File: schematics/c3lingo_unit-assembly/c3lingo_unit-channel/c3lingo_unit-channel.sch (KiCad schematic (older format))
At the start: 124 parts, among them J301 Mic X In, J302 Headphone X, J303 PowerSupply, J304 Inputs, J305 Output, J306 PowerSupply, J307 Interconnect, J308 Interconnect, SW301 OnAir_X, SW302 Mute_X, U301 NE5534, U302 LM833N, U303 LM386N-4, U304 LM833N, U305 LM339, U306 LM339, U307 LM339

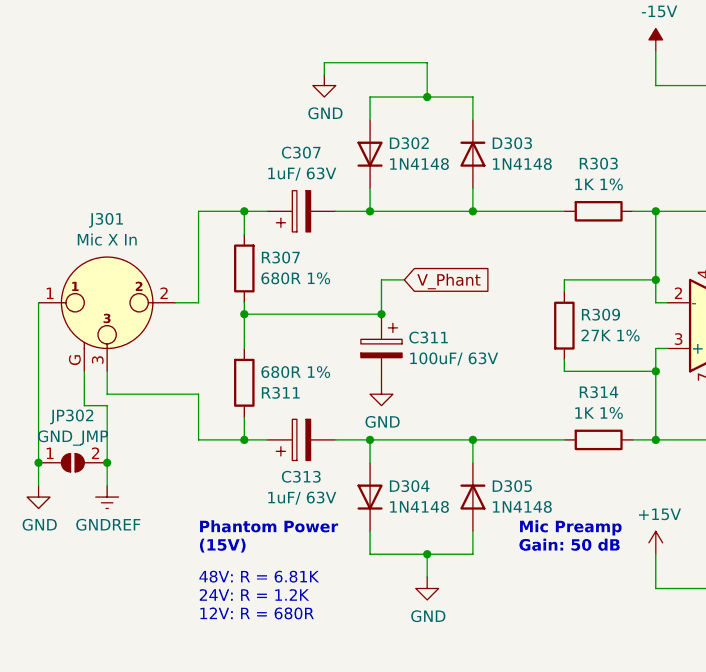
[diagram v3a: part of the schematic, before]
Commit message: PCB: Channel strip design
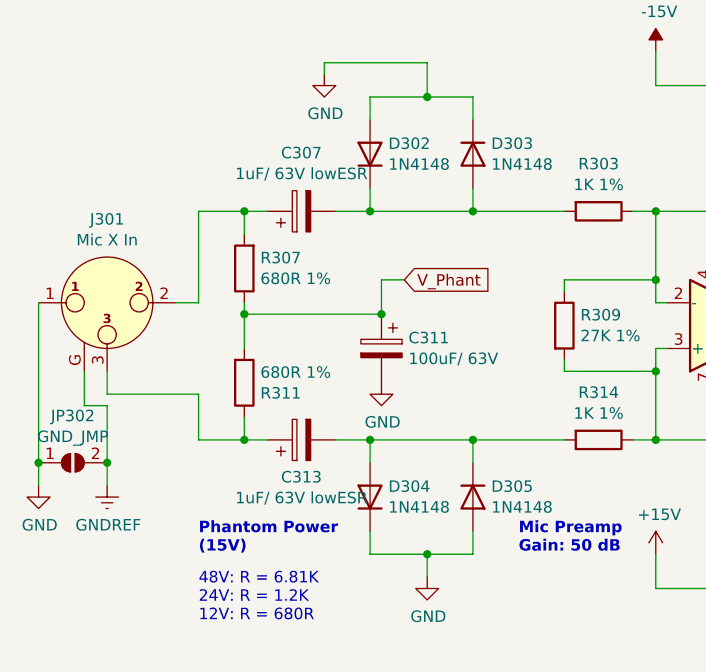
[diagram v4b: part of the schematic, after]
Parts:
- C301, C302, C308, C311, C318: Model 25V -> (none)
- C307, C313: value 1uF/ 63V -> 1uF/ 63V lowESR; Model 16V low ESR electrolytic // plastic film -> low ESR electrolytic // plastic film
- C310: Model 16V low ESR -> (none)
- U301, U302, U303, U304: Model (none) -> +DIP-8 Socket
- U305, U306, U307: Model (none) -> +DIP-14 Socket
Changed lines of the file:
@@
 F 2 "Package_DIP:DIP-14_W7.62mm_Socket_LongPads" H 7050 8500 50  0001 C CNN
 F 3 "https://www.ti.com/lit/ds/symlink/lm339.pdf" H 7150 8600 50  0001 C CNN
+F 4 "+DIP-14 Socket" H 7100 8400 50  0001 C CNN "Model"
 	5    7100 8400
 	0    -1   -1   0
@@
 F 2 "Package_DIP:DIP-14_W7.62mm_Socket_LongPads" H 9650 8500 50  0001 C CNN
 F 3 "https://www.ti.com/lit/ds/symlink/lm339.pdf" H 9750 8600 50  0001 C CNN
+F 4 "+DIP-14 Socket" H 9700 8400 50  0001 C CNN "Model"
 	5    9700 8400
 	0    -1   -1   0
@@
 F 2 "Package_DIP:DIP-14_W7.62mm_Socket_LongPads" H 12250 8500 50  0001 C CNN
 F 3 "https://www.ti.com/lit/ds/symlink/lm339.pdf" H 12350 8600 50  0001 C CNN
+F 4 "+DIP-14 Socket" H 12300 8400 50  0001 C CNN "Model"
 	5    12300 8400
 	0    -1   -1   0
@@
 F 2 "Package_DIP:DIP-8_W7.62mm_Socket_LongPads" H 3050 8600 50  0001 C CNN
 F 3 "https://www.ti.com/lit/ds/symlink/lm833.pdf" H 3050 8600 50  0001 C CNN
+F 4 "+DIP-8 Socket" H 3050 8600 50  0001 C CNN "Model"
 	3    3050 8600
 	0    1    1    0
@@
 F 2 "Package_DIP:DIP-8_W7.62mm_Socket_LongPads" H 3100 7500 50  0001 C CNN
 F 3 "https://www.ti.com/lit/ds/symlink/lm833.pdf" H 3100 7500 50  0001 C CNN
+F 4 "+DIP-8 Socket" H 3100 7500 50  0001 C CNN "Model"
 	2    3100 7500
 	1    0    0    1
@@
 F 2 "Package_DIP:DIP-14_W7.62mm_Socket_LongPads" H 6750 7200 50  0001 C CNN
 F 3 "https://www.ti.com/lit/ds/symlink/lm339.pdf" H 6850 7300 50  0001 C CNN
+F 4 "+DIP-14 Socket" H 6800 7100 50  0001 C CNN "Model"
 	3    6800 7100
 	0    -1   -1   0
@@
 F 2 "Package_DIP:DIP-14_W7.62mm_Socket_LongPads" H 7400 7200 50  0001 C CNN
 F 3 "https://www.ti.com/lit/ds/symlink/lm339.pdf" H 7500 7300 50  0001 C CNN
+F 4 "+DIP-14 Socket" H 7450 7100 50  0001 C CNN "Model"
 	2    7450 7100
 	0    -1   -1   0
@@
 F 2 "Package_DIP:DIP-14_W7.62mm_Socket_LongPads" H 8050 7200 50  0001 C CNN
 F 3 "https://www.ti.com/lit/ds/symlink/lm339.pdf" H 8150 7300 50  0001 C CNN
+F 4 "+DIP-14 Socket" H 8100 7100 50  0001 C CNN "Model"
 	1    8100 7100
 	0    -1   -1   0
@@
 F 2 "Package_DIP:DIP-14_W7.62mm_Socket_LongPads" H 8700 7200 50  0001 C CNN
 F 3 "https://www.ti.com/lit/ds/symlink/lm339.pdf" H 8800 7300 50  0001 C CNN
+F 4 "+DIP-14 Socket" H 8750 7100 50  0001 C CNN "Model"
 	4    8750 7100
 	0    -1   -1   0
@@
 F 2 "Package_DIP:DIP-14_W7.62mm_Socket_LongPads" H 9350 7200 50  0001 C CNN
 F 3 "https://www.ti.com/lit/ds/symlink/lm339.pdf" H 9450 7300 50  0001 C CNN
+F 4 "+DIP-14 Socket" H 9400 7100 50  0001 C CNN "Model"
 	3    9400 7100
 	0    -1   -1   0
@@
 F 2 "Package_DIP:DIP-14_W7.62mm_Socket_LongPads" H 10000 7200 50  0001 C CNN
 F 3 "https://www.ti.com/lit/ds/symlink/lm339.pdf" H 10100 7300 50  0001 C CNN
+F 4 "+DIP-14 Socket" H 10050 7100 50  0001 C CNN "Model"
 	2    10050 7100
 	0    -1   -1   0
@@
 F 2 "Package_DIP:DIP-14_W7.62mm_Socket_LongPads" H 10650 7200 50  0001 C CNN
 F 3 "https://www.ti.com/lit/ds/symlink/lm339.pdf" H 10750 7300 50  0001 C CNN
+F 4 "+DIP-14 Socket" H 10700 7100 50  0001 C CNN "Model"
 	1    10700 7100
 	0    -1   -1   0
@@
 F 2 "Package_DIP:DIP-14_W7.62mm_Socket_LongPads" H 11300 7200 50  0001 C CNN
 F 3 "https://www.ti.com/lit/ds/symlink/lm339.pdf" H 11400 7300 50  0001 C CNN
+F 4 "+DIP-14 Socket" H 11350 7100 50  0001 C CNN "Model"
 	4    11350 7100
 	0    -1   -1   0
@@
 F 2 "Package_DIP:DIP-14_W7.62mm_Socket_LongPads" H 11950 7200 50  0001 C CNN
 F 3 "https://www.ti.com/lit/ds/symlink/lm339.pdf" H 12050 7300 50  0001 C CNN
+F 4 "+DIP-14 Socket" H 12000 7100 50  0001 C CNN "Model"
 	3    12000 7100
 	0    -1   -1   0
@@
 F 2 "Package_DIP:DIP-14_W7.62mm_Socket_LongPads" H 12600 7200 50  0001 C CNN
 F 3 "https://www.ti.com/lit/ds/symlink/lm339.pdf" H 12700 7300 50  0001 C CNN
+F 4 "+DIP-14 Socket" H 12650 7100 50  0001 C CNN "Model"
 	2    12650 7100
 	0    -1   -1   0
@@
 F 2 "Package_DIP:DIP-14_W7.62mm_Socket_LongPads" H 13250 7200 50  0001 C CNN
 F 3 "https://www.ti.com/lit/ds/symlink/lm339.pdf" H 13350 7300 50  0001 C CNN
+F 4 "+DIP-14 Socket" H 13300 7100 50  0001 C CNN "Model"
 	1    13300 7100
 	0    -1   -1   0
@@
 AR Path="/600A9821" Ref="C113"  Part="1"
 F 0 "C313" V 1587 3500 50  0000 C CNN
-F 1 "1uF/ 63V" V 1496 3500 50  0000 C CNN
+F 1 "1uF/ 63V lowESR" V 1496 3500 50  0000 C CNN
 F 2 "Capacitor_THT:CP_Radial_D5.0mm_P2.00mm" H 1788 3350 50  0001 C CNN
 F 3 "~" H 1750 3500 50  0001 C CNN
-F 4 "16V low ESR electrolytic // plastic film" H 1750 3500 50  0001 C CNN "Model"
+F 4 "low ESR electrolytic // plastic film" H 1750 3500 50  0001 C CNN "Model"
 	1    1750 3500
 	0    -1   -1   0
@@
 AR Path="/5FF457A4" Ref="C107"  Part="1"
 F 0 "C307" V 2005 2500 50  0000 C CNN
-F 1 "1uF/ 63V" V 1914 2500 50  0000 C CNN
+F 1 "1uF/ 63V lowESR" V 1914 2500 50  0000 C CNN
 F 2 "Capacitor_THT:CP_Radial_D5.0mm_P2.00mm" H 1788 2350 50  0001 C CNN
 F 3 "~" H 1750 2500 50  0001 C CNN
-F 4 "16V low ESR electrolytic // plastic film" H 1750 2500 50  0001 C CNN "Model"
+F 4 "low ESR electrolytic // plastic film" H 1750 2500 50  0001 C CNN "Model"
 	1    1750 2500
 	0    -1   -1   0
@@
 F 2 "Capacitor_THT:CP_Radial_D10.0mm_P5.00mm" H 2138 2950 50  0001 C CNN
 F 3 "~" H 2100 3100 50  0001 C CNN
-F 4 "25V" H 2100 3100 50  0001 C CNN "Model"
+F 4 "" H 2100 3100 50  0001 C CNN "Model"
 	1    2100 3100
 	-1   0    0    -1
@@
 F 2 "Package_DIP:DIP-8_W7.62mm_Socket_LongPads" H 11750 3000 50  0001 C CNN
 F 3 "https://www.ti.com/lit/ds/symlink/lm833.pdf" H 11750 3000 50  0001 C CNN
+F 4 "+DIP-8 Socket" H 11750 3000 50  0001 C CNN "Model"
 	2    11750 3000
 	1    0    0    1
@@
 F 2 "Package_DIP:DIP-8_W7.62mm_Socket_LongPads" H 14100 3100 50  0001 C CNN
 F 3 "https://www.ti.com/lit/ds/symlink/lm386.pdf" H 14200 3200 50  0001 C CNN
+F 4 "+DIP-8 Socket" H 14000 3000 50  0001 C CNN "Model"
 	1    14000 3000
 	1    0    0    -1
@@
 F 2 "Capacitor_THT:CP_Radial_D6.3mm_P2.50mm" H 14488 1650 50  0001 C CNN
 F 3 "~" H 14450 1800 50  0001 C CNN
-F 4 "25V" H 14450 1800 50  0001 C CNN "Model"
+F 4 "" H 14450 1800 50  0001 C CNN "Model"
 	1    14450 1800
 	0    -1   1    0
@@
 F 2 "Capacitor_THT:CP_Radial_D6.3mm_P2.50mm" H 14188 2400 50  0001 C CNN
 F 3 "~" H 14150 2550 50  0001 C CNN
-F 4 "25V" H 14150 2550 50  0001 C CNN "Model"
+F 4 "" H 14150 2550 50  0001 C CNN "Model"
 	1    14150 2550
 	0    -1   -1   0
@@
 F 2 "Capacitor_THT:CP_Radial_D6.3mm_P2.50mm" H 15088 2850 50  0001 C CNN
 F 3 "~" H 15050 3000 50  0001 C CNN
-F 4 "16V low ESR" H 15050 3000 50  0001 C CNN "Model"
+F 4 "" H 15050 3000 50  0001 C CNN "Model"
 	1    15050 3000
 	0    -1   -1   0
@@
 F 2 "Package_DIP:DIP-8_W7.62mm_Socket_LongPads" H 6800 3250 50  0001 C CNN
 F 3 "https://www.ti.com/lit/ds/symlink/lm833.pdf" H 6800 3250 50  0001 C CNN
+F 4 "+DIP-8 Socket" H 6800 3250 50  0001 C CNN "Model"
 	1    6800 3250
 	1    0    0    1
@@
 F 2 "Package_DIP:DIP-8_W7.62mm_Socket_LongPads" H 8300 4000 50  0001 C CNN
 F 3 "https://www.ti.com/lit/ds/symlink/lm833.pdf" H 8300 4000 50  0001 C CNN
+F 4 "+DIP-8 Socket" H 8300 4000 50  0001 C CNN "Model"
 	3    8300 4000
 	0    1    1    0
@@
 F 2 "Package_DIP:DIP-8_W7.62mm_Socket_LongPads" H 3700 3050 50  0001 C CNN
 F 3 "https://www.ti.com/lit/ds/symlink/ne5534.pdf" H 3700 3150 50  0001 C CNN
+F 4 "+DIP-8 Socket" H 3650 3000 50  0001 C CNN "Model"
 	1    3650 3000
 	1    0    0    1
@@
 F 2 "Capacitor_THT:CP_Radial_D6.3mm_P2.50mm" H 4188 1650 50  0001 C CNN
 F 3 "~" H 4150 1800 50  0001 C CNN
-F 4 "25V" H 4150 1800 50  0001 C CNN "Model"
+F 4 "" H 4150 1800 50  0001 C CNN "Model"
 	1    4150 1800
 	0    1    -1   0
@@
 F 2 "Capacitor_THT:CP_Radial_D6.3mm_P2.50mm" H 4188 4150 50  0001 C CNN
 F 3 "~" H 4150 4300 50  0001 C CNN
-F 4 "25V" H 4150 4300 50  0001 C CNN "Model"
+F 4 "" H 4150 4300 50  0001 C CNN "Model"
 	1    4150 4300
 	0    -1   1    0
@@
 F 2 "Package_DIP:DIP-14_W7.62mm_Socket_LongPads" H 6100 7200 50  0001 C CNN
 F 3 "https://www.ti.com/lit/ds/symlink/lm339.pdf" H 6200 7300 50  0001 C CNN
+F 4 "+DIP-14 Socket" H 6150 7100 50  0001 C CNN "Model"
 	4    6150 7100
 	0    -1   -1   0

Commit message: [FIX] Schematics: Revised values and PCB errata text
* fixed trim pot range at VU meter
* TODOs removed (5V V_LED didn't work out, 10uF at LM386 wasn't better, VU meter filtering not needed)
* phantom power voltage changed and readme chapter added
* hardware errata: gain pot. pins are swapped, ground plane isn't fully connected

Footprints and PCB aren't fixed to keep the schematic compatible with the existing PCBs!
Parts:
- R307, R311: value 680R 1% -> 6.8K 1%
- R320: value 3.9K -> 15K
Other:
- note added: "Bridge V_LED to +15V\n(5V V_LED didn’t work)"
- note added: "Buffer/ Rectifier\nGain: 15\n(3.9 + 12 dB for\ntrim pot. headroom)"
- note added: "DNP R312 and\nreplace C309 with\na jumper!"
- note added: "PCB Errata:\n- R302 (R102 on PCB) has pins 1 and 3 swapped. Connect R305 (R105) directly to the left\n potentiometer pin!\n- The ground plane at the headphone mix potentiometers is not connected to the remaining\n ground plane/ power input. Place a jumper manually!"
- note added: "Phantom Power\n(48V)"
- note added: "Signal Smoothing\n==> DNP (not required)"
- note removed: "Buffer/ Rectifier\nGain: 3.9"
- note removed: "Phantom Power\n(15V)"
- note removed: "Signal Smoothing\nTODO: Remove all together!?"
- note removed: "TODO: Change to 10 uF?"
- note removed: "TODO: Try with V_LED = 5V\nrd: 2.3 V (390R @15V)\ngn: 2.4 V (390R @15V)\nye: 2.6 V (390R @15V)"
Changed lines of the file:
@@
 Sheet 3 5
 Title "c3lingo interpeter unit -- channel strip"
-Date "2021-05-28"
-Rev "v0.2"
+Date "2021-09-02"
+Rev "v0.2.1"
 Comp "Jannik Beyerstedt (jtbx)"
-Comment1 "Prototype 1"
+Comment1 "Prototype 1 (with errata)"
 Comment2 ""
 Comment3 ""
@@
 	0    -1   -1   0
 $EndComp
-Text Notes 1850 7900 0    50   ~ 0
-Buffer/ Rectifier\nGain: 3.9
+Text Notes 1850 8000 0    50   ~ 0
+Buffer/ Rectifier\nGain: 15\n(3.9 + 12 dB for\ntrim pot. headroom)
 $Comp
 L Comparator:LM339 U306
@@
 AR Path="/60B42949" Ref="R120"  Part="1"
 F 0 "R320" V 2843 6500 50  0000 C CNN
-F 1 "3.9K" V 2934 6500 50  0000 C CNN
+F 1 "15K" V 2934 6500 50  0000 C CNN
 F 2 "Resistor_THT:R_Axial_DIN0207_L6.3mm_D2.5mm_P10.16mm_Horizontal" V 2980 6500 50  0001 C CNN
 F 3 "~" H 3050 6500 50  0001 C CNN
@@
 	9900 10800 9900 10500
 Text Notes 4250 8450 0    50   ~ 0
-Signal Smoothing\nTODO: Remove all together!?
+Signal Smoothing\n==> DNP (not required)
 $Comp
 L Device:R R347
@@
 	1    0    0    -1
 $EndComp
-Text Notes 13550 6700 0    50   ~ 0
-TODO: Try with V_LED = 5V\nrd: 2.3 V (390R @15V)\ngn: 2.4 V (390R @15V)\nye: 2.6 V (390R @15V)
 $Comp
 L power:+15V #PWR0329
@@
 $EndComp
 Text Notes 1300 4000 0    50   ~ 10
-Phantom Power\n(15V)
+Phantom Power\n(48V)
 Wire Wire Line
 	1300 3500 1500 3500
@@
 AR Path="/5FDA0F68" Ref="R111"  Part="1"
 F 0 "R311" H 1570 3296 50  0000 L CNN
-F 1 "680R 1%" H 1570 3205 50  0000 L CNN
+F 1 "6.8K 1%" H 1570 3205 50  0000 L CNN
 F 2 "Resistor_THT:R_Axial_DIN0207_L6.3mm_D2.5mm_P10.16mm_Horizontal" V 1430 3250 50  0001 C CNN
 F 3 "~" H 1500 3250 50  0001 C CNN
@@
 AR Path="/5FD87CA8" Ref="R107"  Part="1"
 F 0 "R307" H 1430 2704 50  0000 R CNN
-F 1 "680R 1%" H 1430 2795 50  0000 R CNN
+F 1 "6.8K 1%" H 1430 2795 50  0000 R CNN
 F 2 "Resistor_THT:R_Axial_DIN0207_L6.3mm_D2.5mm_P10.16mm_Horizontal" V 1430 2750 50  0001 C CNN
 F 3 "~" H 1500 2750 50  0001 C CNN
@@
 	-1   0    0    -1
 $EndComp
-Text Notes 14400 2500 0    50   ~ 0
-TODO: Change to 10 uF?
 Wire Wire Line
 	13500 2900 13500 3650
@@
 	1    0    0    -1
 $EndComp
+Text Notes 11800 9900 0    58   ~ 12
+PCB Errata:\n- R302 (R102 on PCB) has pins 1 and 3 swapped. Connect R305 (R105) directly to the left\n   potentiometer pin!\n- The ground plane at the headphone mix potentiometers is not connected to the remaining\n   ground plane/ power input. Place a jumper manually!
+Text Notes 4650 3750 0    50   ~ 0
+DNP R312 and\nreplace C309 with\na jumper!
+Text Notes 8000 10200 0    50   ~ 0
+Bridge V_LED to +15V\n(5V V_LED didn’t work)
 $EndSCHEMATC
